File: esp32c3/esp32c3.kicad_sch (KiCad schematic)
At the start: 29 parts, among them J1 A1501WR-S-2P, J2 Conn_01x06, J3 Conn_01x05, SW1 wake up, U1 ESP32-C3-WROOM-02, U2 AHT10, U3 LIS2DH, U4 HX6306

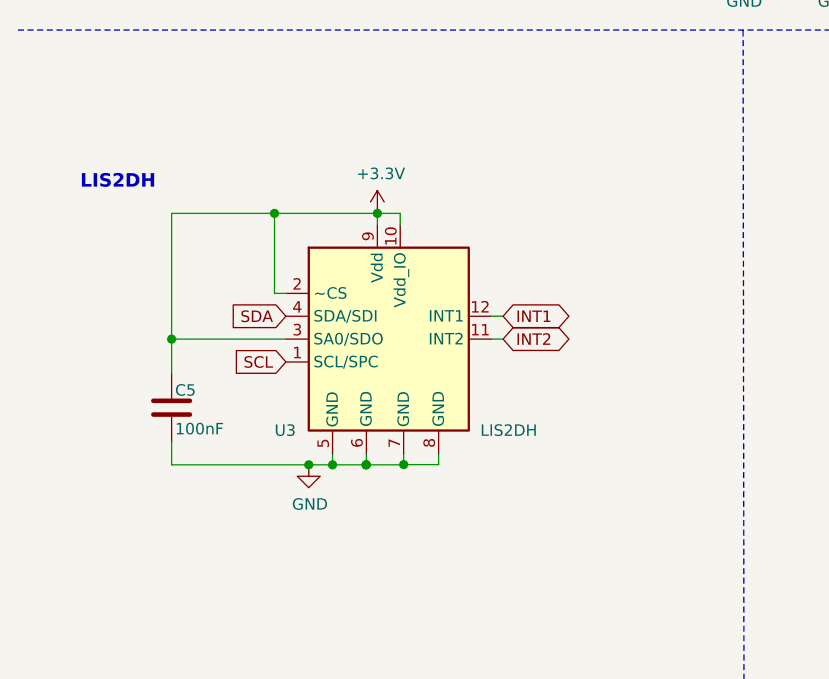
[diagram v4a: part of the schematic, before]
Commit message: Complete LIS2DH12 modification
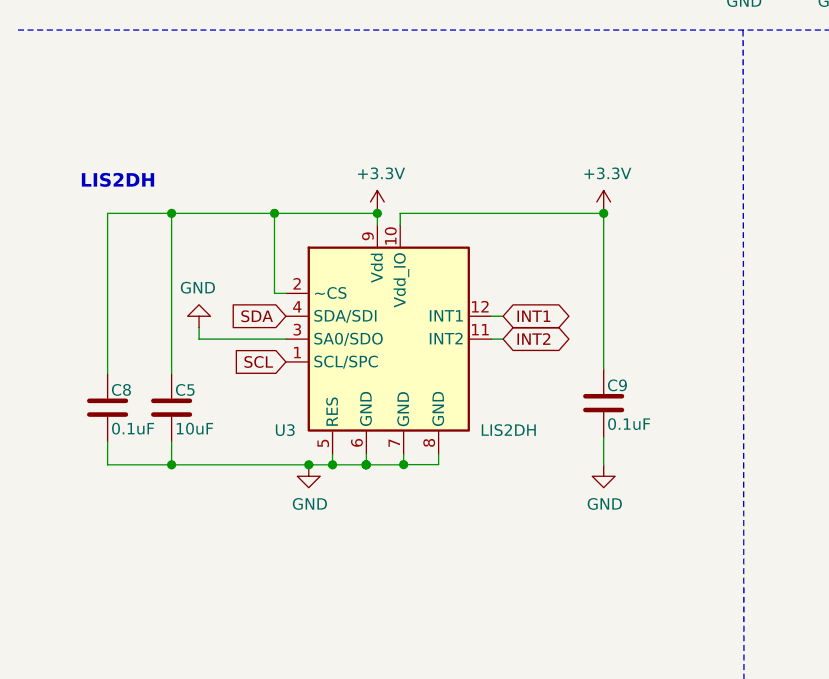
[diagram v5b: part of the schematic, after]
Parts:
- added C8, C9: 0.1uF, Resistor_SMD:R_0603_1608Metric_Pad0.98x0.95mm_HandSolder, symbol Device:C
- C5: value 100nF -> 10uF
- U3: footprint Package_LGA:LGA-14_2x2mm_P0.35mm_LayoutBorder3x4y -> Package_LGA:LGA-12_2x2mm_P0.5mm
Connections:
- net +3V3: now also C8.1, C9.1; no longer U3.3 (SA0/SDO)
- net GND: now also U3.3 (SA0/SDO), C8.2, C9.2
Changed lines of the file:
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@@
   )
   (junction (at 29.21 68.58) (diameter 1.016) (color 0 0 0 0))
-  (junction (at 29.21 120.65) (diameter 1.016) (color 0 0 0 0))
+  (junction (at 29.21 106.68) (diameter 1.016) (color 0 0 0 0))
+  (junction (at 29.21 134.62) (diameter 1.016) (color 0 0 0 0))
   (junction (at 30.48 177.8) (diameter 1.016) (color 0 0 0 0))
   (junction (at 40.64 106.68) (diameter 1.016) (color 0 0 0 0))
@@
   (junction (at 54.991 134.5946) (diameter 1.016) (color 0 0 0 0))
   (junction (at 59.69 177.8) (diameter 1.016) (color 0 0 0 0))
+  (junction (at 77.216 106.68) (diameter 1.016) (color 0 0 0 0))
   (junction (at 87.63 35.56) (diameter 1.016) (color 0 0 0 0))
   (junction (at 87.63 48.26) (diameter 1.016) (color 0 0 0 0))
@@
   (no_connect (at 175.006 111.76))
   (no_connect (at 185.674 111.76))
+  (wire (pts (xy 22.098 106.68) (xy 29.21 106.68))
+    (stroke (width 0) (type solid) (color 0 0 0 0))
+  )
+  (wire (pts (xy 22.098 124.46) (xy 22.098 106.68))
+    (stroke (width 0) (type solid) (color 0 0 0 0))
+  )
+  (wire (pts (xy 22.098 134.62) (xy 22.098 132.08))
+    (stroke (width 0) (type solid) (color 0 0 0 0))
+  )
   (wire (pts (xy 25.4 38.1) (xy 31.75 38.1))
     (stroke (width 0) (type solid) (color 0 0 0 0))
@@
     (stroke (width 0) (type solid) (color 0 0 0 0))
   )
-  (wire (pts (xy 29.21 106.68) (xy 29.21 120.65))
+  (wire (pts (xy 29.21 106.68) (xy 29.21 124.46))
     (stroke (width 0) (type solid) (color 0 0 0 0))
   )
@@
     (stroke (width 0) (type solid) (color 0 0 0 0))
   )
-  (wire (pts (xy 29.21 120.65) (xy 29.21 124.46))
-    (stroke (width 0) (type solid) (color 0 0 0 0))
-  )
   (wire (pts (xy 29.21 132.08) (xy 29.21 134.62))
     (stroke (width 0) (type solid) (color 0 0 0 0))
   )
+  (wire (pts (xy 29.21 134.62) (xy 22.098 134.62))
+    (stroke (width 0) (type solid) (color 0 0 0 0))
+  )
   (wire (pts (xy 29.21 134.62) (xy 44.45 134.62))
     (stroke (width 0) (type solid) (color 0 0 0 0))
@@
     (stroke (width 0) (type solid) (color 0 0 0 0))
   )
+  (wire (pts (xy 32.258 120.65) (xy 32.258 119.38))
+    (stroke (width 0) (type solid) (color 0 0 0 0))
+  )
   (wire (pts (xy 33.02 177.8) (xy 30.48 177.8))
     (stroke (width 0) (type solid) (color 0 0 0 0))
@@
     (stroke (width 0) (type solid) (color 0 0 0 0))
   )
-  (wire (pts (xy 41.91 120.65) (xy 29.21 120.65))
+  (wire (pts (xy 41.91 120.65) (xy 32.258 120.65))
     (stroke (width 0) (type solid) (color 0 0 0 0))
   )
@@
     (stroke (width 0) (type solid) (color 0 0 0 0))
   )
-  (wire (pts (xy 52.07 106.68) (xy 54.61 106.68))
-    (stroke (width 0) (type solid) (color 0 0 0 0))
-  )
   (wire (pts (xy 52.07 107.95) (xy 52.07 106.68))
     (stroke (width 0) (type solid) (color 0 0 0 0))
@@
     (stroke (width 0) (type solid) (color 0 0 0 0))
   )
+  (wire (pts (xy 54.61 106.68) (xy 77.216 106.68))
+    (stroke (width 0) (type solid) (color 0 0 0 0))
+  )
   (wire (pts (xy 54.991 133.477) (xy 54.991 134.5946))
     (stroke (width 0) (type solid) (color 0 0 0 0))
@@
   )
   (wire (pts (xy 69.85 186.69) (xy 72.39 186.69))
+    (stroke (width 0) (type solid) (color 0 0 0 0))
+  )
+  (wire (pts (xy 77.216 106.68) (xy 77.216 123.952))
+    (stroke (width 0) (type solid) (color 0 0 0 0))
+  )
+  (wire (pts (xy 77.216 131.572) (xy 77.216 134.62))
     (stroke (width 0) (type solid) (color 0 0 0 0))
   )
@@
     (pin "1")
   )
+  (symbol (lib_id "e-tinkers-esp32-c3-rescue:+3.3V-power") (at 77.216 106.68 0) (unit 1)
+    (in_bom yes) (on_board yes)
+    (property "Reference" "#PWR0132" (id 0) (at 77.216 110.49 0)
+      (effects (font (size 1.27 1.27)) hide)
+    )
+    (property "Value" "+3.3V" (id 1) (at 77.597 102.2858 0))
+    (property "Footprint" "" (id 2) (at 77.216 106.68 0)
+      (effects (font (size 1.27 1.27)) hide)
+    )
+    (property "Datasheet" "" (id 3) (at 77.216 106.68 0)
+      (effects (font (size 1.27 1.27)) hide)
+    )
+    (pin "1")
+  )
   (symbol (lib_id "e-tinkers-esp32-c3-rescue:+3.3V-power") (at 87.63 34.29 0) (unit 1)
     (in_bom yes) (on_board yes)
@@
     (pin "1")
   )
+  (symbol (lib_id "power:GND") (at 32.258 119.38 180) (unit 1)
+    (in_bom yes) (on_board yes)
+    (property "Reference" "#PWR0131" (id 0) (at 32.258 113.03 0)
+      (effects (font (size 1.27 1.27)) hide)
+    )
+    (property "Value" "GND" (id 1) (at 32.131 114.9858 0))
+    (property "Footprint" "" (id 2) (at 32.258 119.38 0)
+      (effects (font (size 1.27 1.27)) hide)
+    )
+    (property "Datasheet" "" (id 3) (at 32.258 119.38 0)
+      (effects (font (size 1.27 1.27)) hide)
+    )
+    (pin "1")
+  )
   (symbol (lib_id "power:GND") (at 43.18 177.8 90) (unit 1)
     (in_bom yes) (on_board yes)
@@
     )
     (property "Datasheet" "" (id 3) (at 72.39 177.8 0)
+      (effects (font (size 1.27 1.27)) hide)
+    )
+    (pin "1")
+  )
+  (symbol (lib_id "power:GND") (at 77.216 134.62 0) (unit 1)
+    (in_bom yes) (on_board yes)
+    (property "Reference" "#PWR?" (id 0) (at 77.216 140.97 0)
+      (effects (font (size 1.27 1.27)) hide)
+    )
+    (property "Value" "GND" (id 1) (at 77.343 139.0142 0))
+    (property "Footprint" "" (id 2) (at 77.216 134.62 0)
+      (effects (font (size 1.27 1.27)) hide)
+    )
+    (property "Datasheet" "" (id 3) (at 77.216 134.62 0)
       (effects (font (size 1.27 1.27)) hide)
     )
@@
     (pin "2")
   )
+  (symbol (lib_name "Device:C_1") (lib_id "Device:C") (at 22.098 128.27 0) (unit 1)
+    (in_bom yes) (on_board yes)
+    (property "Reference" "C8" (id 0) (at 22.4791 126.3455 0)
+      (effects (font (size 1.27 1.27)) (justify left))
+    )
+    (property "Value" "0.1uF" (id 1) (at 22.4791 130.6446 0)
+      (effects (font (size 1.27 1.27)) (justify left))
+    )
+    (property "Footprint" "Resistor_SMD:R_0603_1608Metric_Pad0.98x0.95mm_HandSolder" (id 2) (at 23.0632 132.08 0)
+      (effects (font (size 1.27 1.27)) hide)
+    )
+    (property "Datasheet" "~" (id 3) (at 22.098 128.27 0)
+      (effects (font (size 1.27 1.27)) hide)
+    )
+    (pin "1")
+    (pin "2")
+  )
   (symbol (lib_name "Device:C_1") (lib_id "Device:C") (at 29.21 128.27 0) (unit 1)
     (in_bom yes) (on_board yes)
@@
       (effects (font (size 1.27 1.27)) (justify left))
     )
-    (property "Value" "100nF" (id 1) (at 29.5911 130.6446 0)
+    (property "Value" "10uF" (id 1) (at 29.5911 130.6446 0)
       (effects (font (size 1.27 1.27)) (justify left))
     )
@@
     )
     (property "Datasheet" "~" (id 3) (at 29.21 128.27 0)
+      (effects (font (size 1.27 1.27)) hide)
+    )
+    (pin "1")
+    (pin "2")
+  )
+  (symbol (lib_name "Device:C_1") (lib_id "Device:C") (at 77.216 127.762 0) (unit 1)
+    (in_bom yes) (on_board yes)
+    (property "Reference" "C9" (id 0) (at 77.5971 125.8375 0)
+      (effects (font (size 1.27 1.27)) (justify left))
+    )
+    (property "Value" "0.1uF" (id 1) (at 77.5971 130.1366 0)
+      (effects (font (size 1.27 1.27)) (justify left))
+    )
+    (property "Footprint" "Resistor_SMD:R_0603_1608Metric_Pad0.98x0.95mm_HandSolder" (id 2) (at 78.1812 131.572 0)
+      (effects (font (size 1.27 1.27)) hide)
+    )
+    (property "Datasheet" "~" (id 3) (at 77.216 127.762 0)
       (effects (font (size 1.27 1.27)) hide)
     )
@@
       (effects (font (size 1.27 1.27)) (justify left))
     )
-    (property "Footprint" "Package_LGA:LGA-14_2x2mm_P0.35mm_LayoutBorder3x4y" (id 2) (at 52.07 135.89 0)
+    (property "Footprint" "Package_LGA:LGA-12_2x2mm_P0.5mm" (id 2) (at 52.07 135.89 0)
       (effects (font (size 1.27 1.27)) hide)
     )
@@
       (reference "#PWR0130") (unit 1) (value "GND") (footprint "")
     )
+    (path "/045f0683-5bf1-45a9-8d7d-c164564262b6"
+      (reference "#PWR0131") (unit 1) (value "GND") (footprint "")
+    )
+    (path "/1727889e-ba20-4a1c-8bf4-b1bfbbda3c7a"
+      (reference "#PWR0132") (unit 1) (value "+3.3V") (footprint "")
+    )
+    (path "/45e32586-cb5a-4f31-95a6-338557705273"
+      (reference "#PWR?") (unit 1) (value "GND") (footprint "")
+    )
     (path "/c8a6d50c-4ea1-48ee-a734-16ae94915e8a"
       (reference "C1") (unit 1) (value "10uF") (footprint "Resistor_SMD:R_0603_1608Metric_Pad0.98x0.95mm_HandSolder")
@@
     )
     (path "/504b111b-94f9-45d4-a954-66b8f721a624"
-      (reference "C5") (unit 1) (value "100nF") (footprint "Resistor_SMD:R_0603_1608Metric_Pad0.98x0.95mm_HandSolder")
+      (reference "C5") (unit 1) (value "10uF") (footprint "Resistor_SMD:R_0603_1608Metric_Pad0.98x0.95mm_HandSolder")
     )
     (path "/8f8fe057-4458-46af-9634-f0cee6c2466a"
@@
       (reference "C7") (unit 1) (value "1uF") (footprint "Resistor_SMD:R_0603_1608Metric_Pad0.98x0.95mm_HandSolder")
     )
+    (path "/71f5ba04-aec6-4177-a78c-e0c7f29b4ec3"
+      (reference "C8") (unit 1) (value "0.1uF") (footprint "Resistor_SMD:R_0603_1608Metric_Pad0.98x0.95mm_HandSolder")
+    )
+    (path "/2936c9a2-5c3a-4fe9-9a6d-fe2a08a9419b"
+      (reference "C9") (unit 1) (value "0.1uF") (footprint "Resistor_SMD:R_0603_1608Metric_Pad0.98x0.95mm_HandSolder")
+    )
     (path "/63a6797f-821f-49f7-9cf4-4edd85d04a8f"
       (reference "D1") (unit 1) (value "LED_RED") (footprint "LED_SMD:LED_0805_2012Metric")
@@
     )
     (path "/bacb6c10-c04e-42e3-94c0-aad3bde5f03c"
-      (reference "U3") (unit 1) (value "LIS2DH") (footprint "Package_LGA:LGA-14_2x2mm_P0.35mm_LayoutBorder3x4y")
+      (reference "U3") (unit 1) (value "LIS2DH") (footprint "Package_LGA:LGA-12_2x2mm_P0.5mm")
     )
     (path "/e58fd954-d353-4b6e-9f67-9f64a10351c4"

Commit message: prepare v2.0-alpha-1 for fabrication
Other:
- note added: "LIS2DH12"
- note added: "bovi[2022-04-22]: DTR to TXD etc. is probably a bug"
- note added: "bovi[2022-04-22]: this component doesn't seem ROHS compliant."
- note added: "bovi[2022-04-22]: we probably need to migrate to mini"
- note added: "bovi[2022-04-22]: we probably need two LDOs"
- note removed: "LIS2DH"
- company: Siemens -> Siemens Ltd. China
- title: ESP32-C3-WROOM-02 -> MindDot
